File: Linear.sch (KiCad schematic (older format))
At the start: 50 parts, among them Q11 4403, Q6 D45H11, Q7 MMBT3904, Q8 PZT3904, U1 AD8602ARZ, U2 LM358M, U3 LM393M, U4 SN74LVC2G14DBV, U5 LM393M

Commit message: First working version
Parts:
- removed C48: 100n, IPC7351-Nominal:CAPC1608X55, symbol C-0603
- removed R23: 470k, IPC7351-Nominal:RESC1608X50, symbol R-0603
- removed U4: SN74LVC2G14DBV, smd-semi:SOT-23-6, symbol SN74LVC2G14DBV
- added C54: 100n, IPC7351-Nominal:CAPC1608X55, symbol C-0603
- added D3: BAT54AWT, smd-semi:SC-70, symbol BAT54AWT
- added E5: 120, IPC7351-Nominal:INDC1608X95, symbol BEAD-0603
- added Q12: 2N7002PW, smd-semi:SC-70, symbol 2N7002PW
- added R57: 348, IPC7351-Nominal:RESC1608X50, symbol R-0603
- added R58: 22k, IPC7351-Nominal:RESC1608X50, symbol R-0603
- C10: value 220p -> 22n; BOM CAP MLCC 220p C0G 50V 10% [0603] -> CAP MLCC 22n ≥X5R 50V 10% [0603]
- C11: value 22n -> 220p; BOM CAP MLCC 22n ≥X5R 50V 10% [0603] -> CAP MLCC 220p C0G 50V 10% [0603]
- DZ1: value 84C24 -> 84B24; BOM (none) -> DIST DIGIKEY 568-8063-1-ND
- R12, R15, R18, R38, R8, R9: value 20k -> 22k; BOM RES SMD 20k 1% [0603] -> RES SMD 22k 1% [0603]
- R13: value 330 -> 348; BOM RES SMD 330 1% [0603] -> RES SMD 348 1% [0603]
- R24: value 20k -> 2k; BOM RES SMD 20k 1% [0603] -> RES SMD 2k 1% [0603]
- R28: value 2k -> 348; BOM RES SMD 2k 1% [0603] -> RES SMD 348 1% [0603]
- R37: value 470k -> 22k; BOM RES SMD 470k 5% [0603] -> RES SMD 22k 1% [0603]
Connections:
- net GND: now also C54.1, Q12.2
- net P_OUT: now also E5.1; no longer Q8.3, R22.1
- net V+: now also R58.1
- net VSENSE+: now also R7.2, R9.2; no longer R6.2, R8.2
- net VSENSE-: now also R6.2, R8.2; no longer R7.2, R9.2
- net ~VLIM: now reaches C14.2, R29.1, U3.1 (OUT)
- net at D2.3, U3.2 (IN-), U3.6 (IN-): now also Q12.3, R57.1; no longer Q7.1, R18.2
- net ~ILIM: now reaches C15.2, R31.1, U3.7 (OUT)
- net at Q7.2, Q8.1, R22.2: now also D3.1
- net at R25.1, U5.3 (IN+): now also C54.2
- new net: D3.3, E5.2, Q8.3, R22.1
- new net: D3.2, Q7.1, R18.2, R57.2
- new net ~EN: Q12.1, R58.2
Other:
- note added: "490mV"
- note added: "AD8606"
- note added: "Ratio: 64.2"
- note added: "Separate VLIM and ILIM signals with asymmetric\nrise/fall allows detection of CC/CV oscillations\nfaster than the controller's scan rate.\n\nIn the case of oscillation, both limit signals will\nbe low. This requires an input with hysteresis,\nwhich the XMEGA E5 has on all GPIOs."
- moved on the sheet: C42, C43, C44, C45, C47, C50, Q7, Q8, R18, R19, R22, R24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

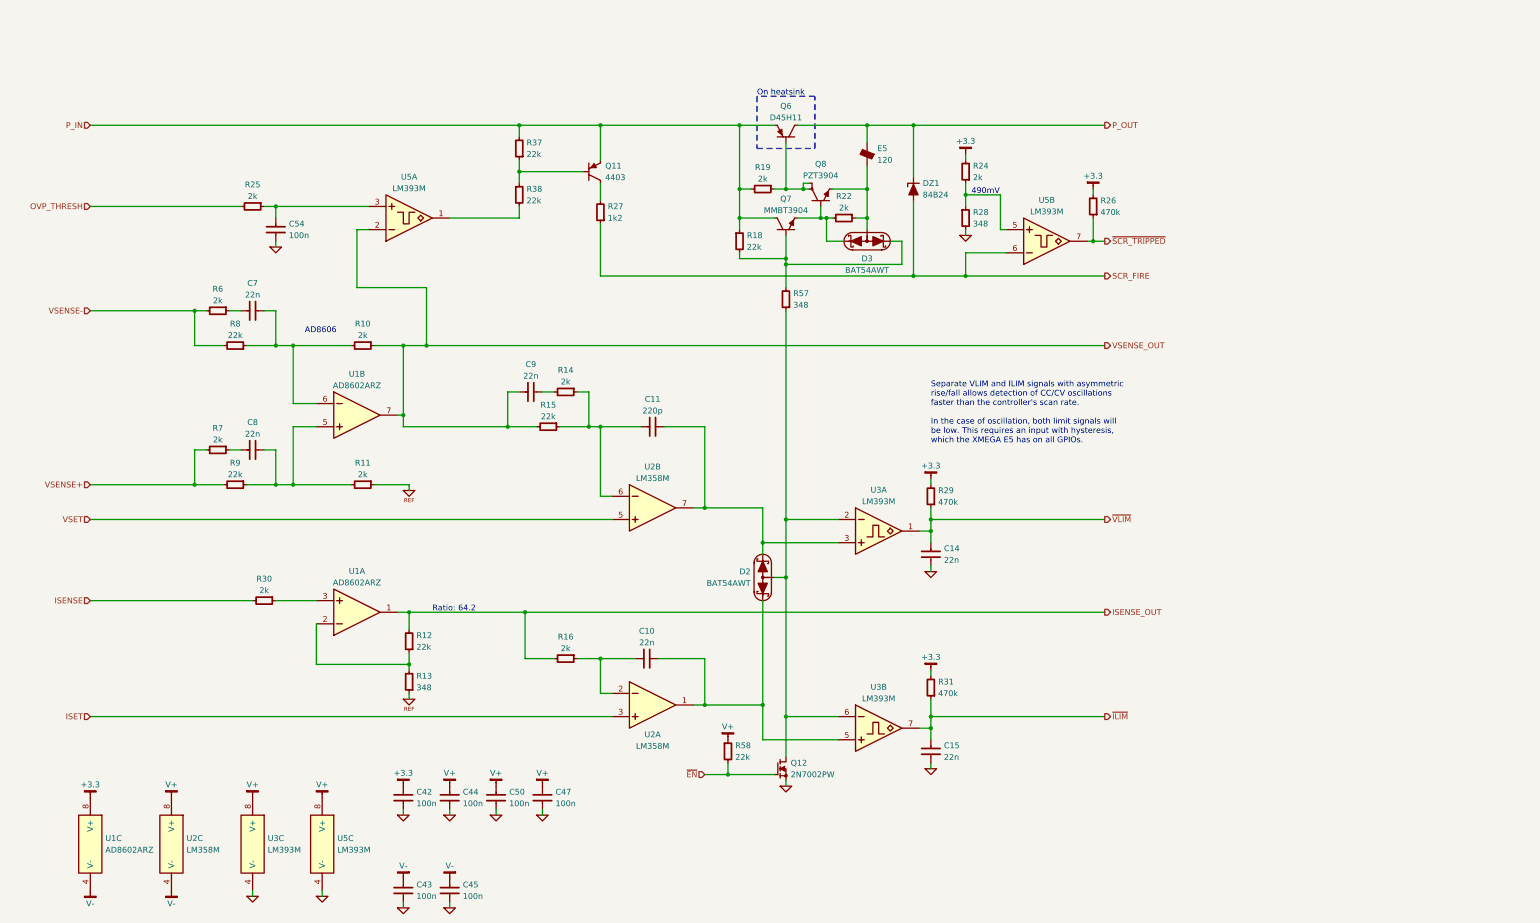
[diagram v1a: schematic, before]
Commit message: Reannotate component references
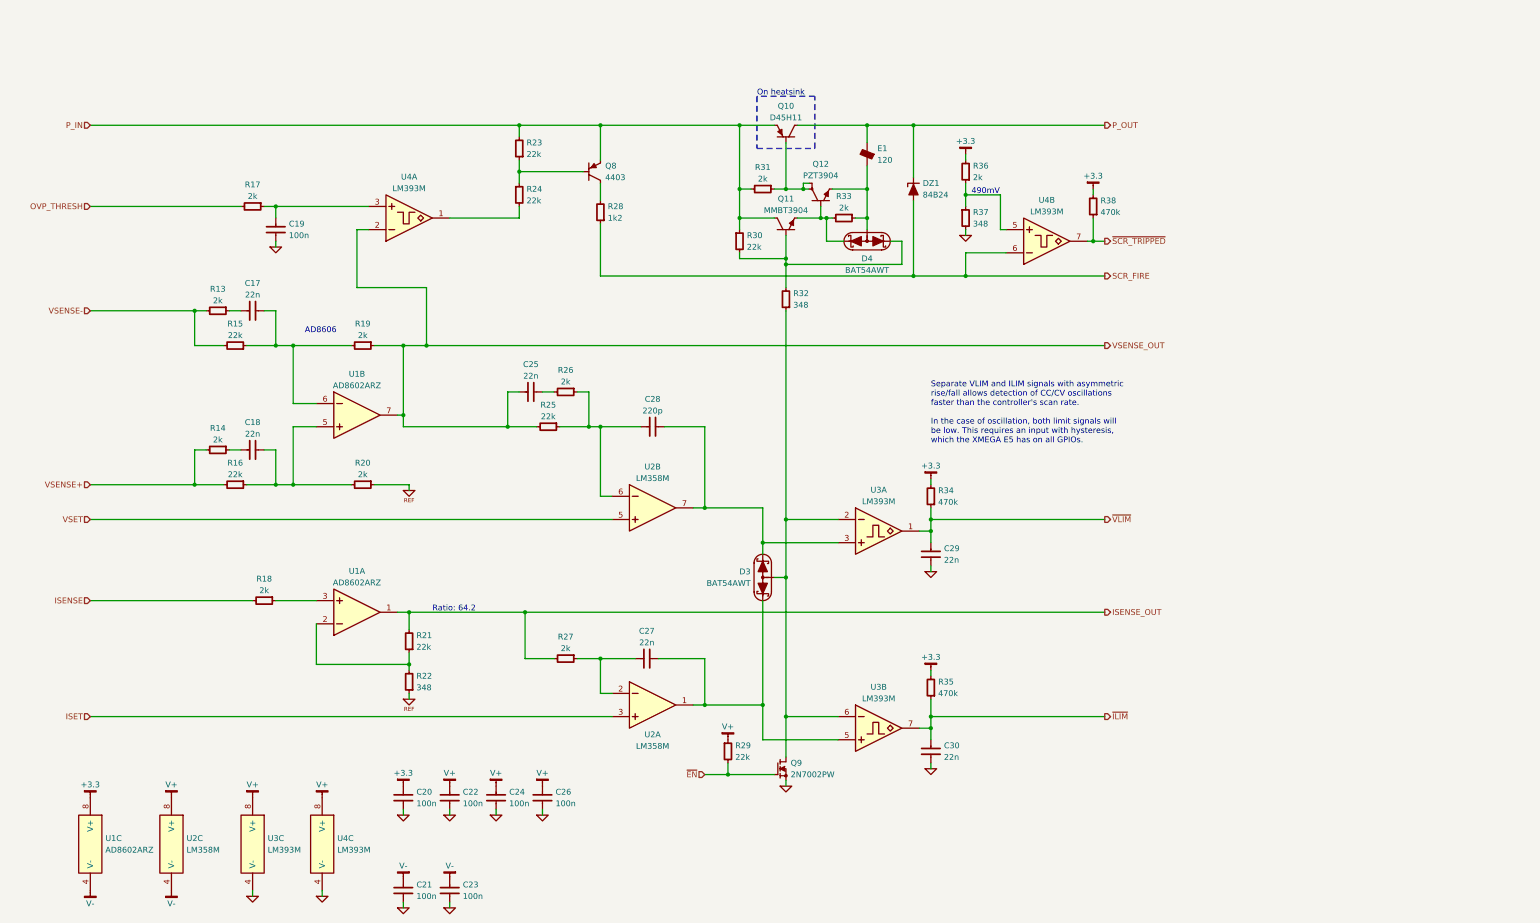
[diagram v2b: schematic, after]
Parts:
- renumbered C7 to C17, C8 to C18, C54 to C19, C42 to C20, C43 to C21, C44 to C22, C45 to C23, C50 to C24, C9 to C25, C47 to C26, C10 to C27, C11 to C28, C14 to C29, C15 to C30, D2 to D3, D3 to D4, E5 to E1, Q6 to Q10, Q7 to Q11, Q8 to Q12, Q11 to Q8, Q12 to Q9, R6 to R13, R7 to R14, R8 to R15, R9 to R16, R25 to R17, R30 to R18, R10 to R19, R11 to R20, R12 to R21, R13 to R22, R37 to R23, R38 to R24, R15 to R25, R14 to R26, R16 to R27, R27 to R28, R58 to R29, R18 to R30, R19 to R31, R57 to R32, R22 to R33, R29 to R34, R31 to R35, R24 to R36, R28 to R37, R26 to R38, U5 to U4

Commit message: Piles and piles of work
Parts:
- removed U1: AD8602ARZ, IPC7351-Nominal:SOIC127P600X175-8, symbol AD8602ARZ
- added TP10: ISET, conn-test:TEST-SMD-SMALL, symbol TESTPOINT
- added TP11: VDRIVE, conn-test:TEST-SMD-SMALL, symbol TESTPOINT
- added TP12: IDRIVE, conn-test:TEST-SMD-SMALL, symbol TESTPOINT
- added TP13: DRIVE, conn-test:TEST-SMD-SMALL, symbol TESTPOINT
- added TP6: OVP_TH, conn-test:TEST-SMD-SMALL, symbol TESTPOINT
- added TP7: VSENSE, conn-test:TEST-SMD-SMALL, symbol TESTPOINT
- added TP8: VSET, conn-test:TEST-SMD-SMALL, symbol TESTPOINT
- added TP9: ISENSE, conn-test:TEST-SMD-SMALL, symbol TESTPOINT
- added U1: OPA2376AID, IPC7351-Nominal:SOIC127P600X175-8, symbol OPA2376AID
- Q12: BOM (none) -> NPN PZT3904
- R28: value 1k2 -> 1k; BOM RES SMD 1k2 5% [2512] -> RES SMD 1k [2512]
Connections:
- net +3.3: now also U1.8 (V+)
- net ISENSE_OUT: now also TP9.1, U1.1 (OUT)
- net ISET: now also TP10.1
- net OVP_THRESH: now also TP6.1
- net V-: now also U1.4 (V-)
- net VSENSE_OUT: now also TP7.1, U1.7 (OUT)
- net VSET: now also TP8.1
- net at C28.1, D3.2, U2.7 (OUT)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: now also TP11.1
- net at C27.1, D3.1, U2.1 (OUT)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: now also TP12.1
- net at C18.1, R16.1, R20.2: now also U1.5 (IN+)
- net at C17.1, R15.1, R19.2: now also U1.6 (IN-)
- net at R21.1, R22.2: now also U1.2 (IN-)
- net at R18.1: now also U1.3 (IN+)
- net at D3.3, Q9.3, R32.1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: now also TP13.1
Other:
- note added: "(0.01V)"
- note added: "(0.05V)"
- note added: "(0.49V)"
- note added: "(0.64V)"
- note added: "(0.96V)"
- note added: "(1.09V)"
- note added: "(1.36V)"
- note added: "(12.00V)"
- note added: "(12.01V)"
- note added: "(12.65V)"
- note added: "(13.00V)"
- note added: "(13.30V)"
- note added: "(13.77V)"
- note added: "(14.50V)"
- note added: "(23.00V)"
- note added: "(3.30V)"
- note added: "Av=64.22"
- note added: "PROBE POINT FOR ISENSE:\nDirectly across R3"
- note added: "PROBE POINT FOR VSENSE+/-:\nDirectly across output connectors"
- note added: "Test conditions:\nVout = 12V Vovp = 15V\nIout = 1A Ilim = 1.5A"
- note removed: "490mV"
- note removed: "AD8606"
- note removed: "Ratio: 64.2"
- moved on the sheet: C25, E1, Q12, R25, R26, R30, R31, R38
